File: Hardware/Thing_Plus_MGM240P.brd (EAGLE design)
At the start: 22.9 x 58.4 mm, 175 parts, among them J1 THING_PLUS_LOGICAL, J2 USB Female Type C Connector, J3 QWIIC_RIGHT_ANGLE, J5 MICRO-SDFRICTION, Q1 20V/4.2A/52mΩ/1.4W, U1 MGM240P, U2 XC6222B331MR-G, U3 EFM32GG12B410F1024GL120, U4 MCP73831, U5 MAX17048, U6 M24C02-FMC6TG, U7 MX25R8035FZUIL0, Y1 CRYSTAL-48MHZ

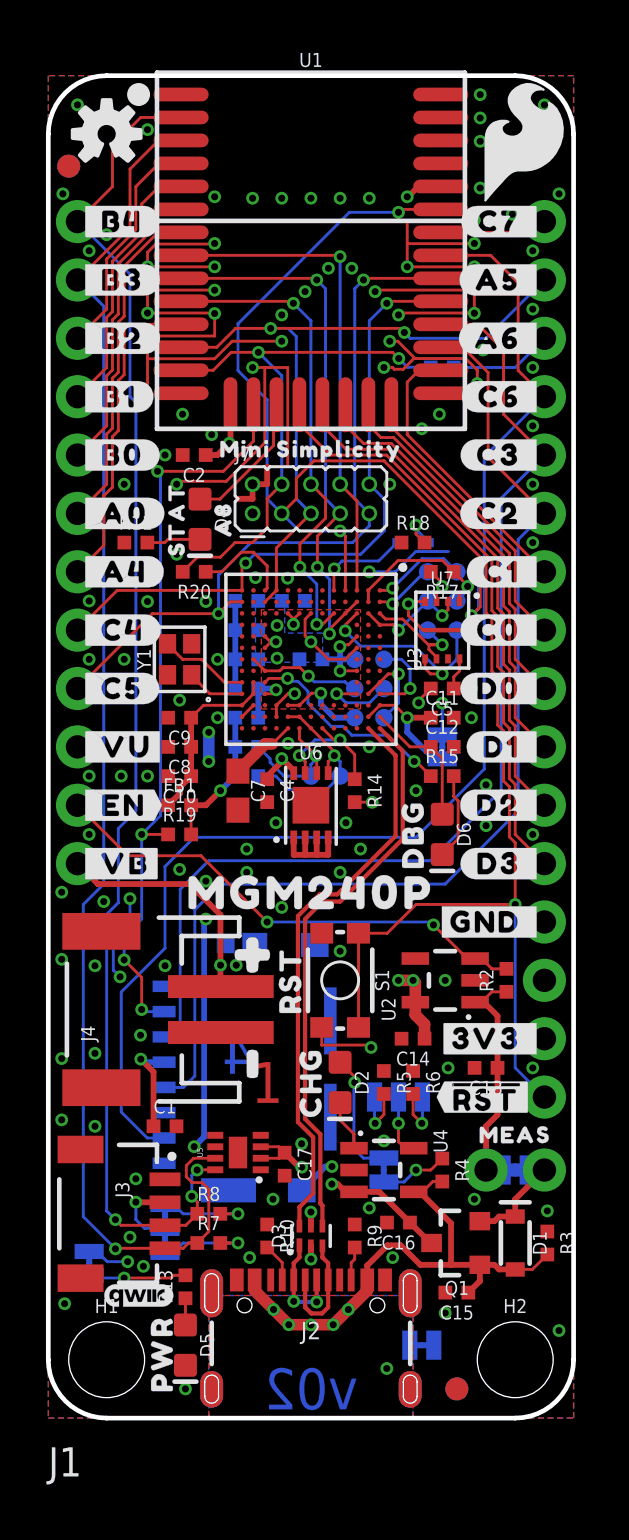
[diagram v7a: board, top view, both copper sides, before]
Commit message: Design review updates
Change voltage regulator to specify maximum input voltage only
Add Segger logo
Move traces away from jumpers to prevent accidental cutting
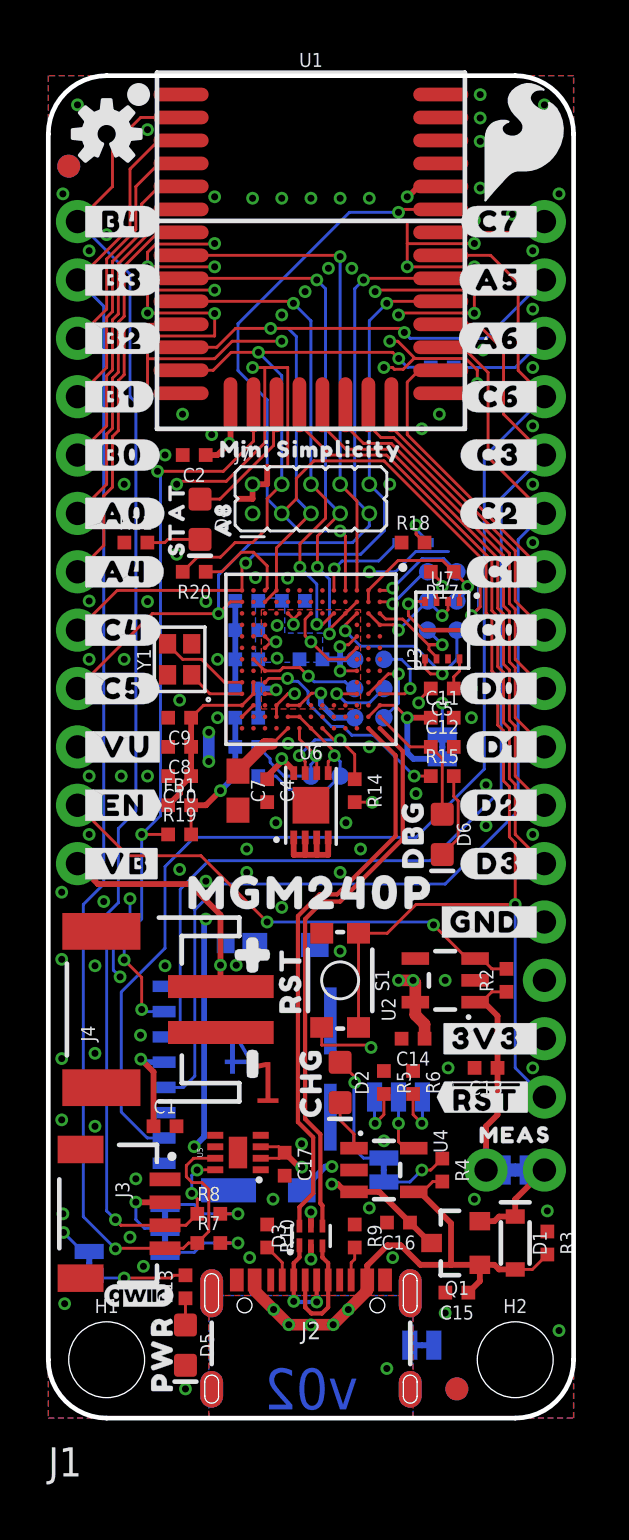
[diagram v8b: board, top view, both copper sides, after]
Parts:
- added U$65: (no value), SEGGER-LOGO:SEGGER_LOGO
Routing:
- net V_USB: track 49.6 -> 50.1 mm
- net GND: vias 136 -> 137
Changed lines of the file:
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@@
 <attribute name="VALUE" x="17.145" y="45.158" size="0.6096" layer="28" font="vector" ratio="20" rot="MR0" align="top-center"/>
 </element>
+<element name="U$65" library="SEGGER-LOGO" package="SEGGER_LOGO" value="" x="9.65" y="44.45" smashed="yes" rot="MR0"/>
 </elements>
 <signals>
@@
 <via x="13.97" y="29.21" extent="1-16" drill="0.3048"/>
 <via x="12.954" y="25.908" extent="1-16" drill="0.3048"/>
-<via x="16.002" y="27.305" extent="1-16" drill="0.3048"/>
+<via x="16.002" y="27.178" extent="1-16" drill="0.3048"/>
 <via x="10.414" y="36.5506" extent="1-16" drill="0.3048"/>
 <via x="13.97" y="36.83" extent="1-16" drill="0.3048"/>
@@
 <via x="4.318" y="35.5346" extent="1-16" drill="0.3048"/>
 <via x="21.082" y="25.4" extent="1-16" drill="0.3048"/>
+<via x="0.635" y="8.89" extent="1-16" drill="0.3048"/>
 </signal>
 <signal name="3.3V">
@@
 <wire x1="4.1569" y1="15.49" x2="4.0259" y2="15.621" width="0.254" layer="16"/>
 <via x="4.0259" y="15.621" extent="1-16" drill="0.3048"/>
-<via x="3.4544" y="6.8072" extent="1-16" drill="0.3048"/>
+<via x="0.6604" y="8.0772" extent="1-16" drill="0.3048"/>
 <contactref element="C1" pad="1"/>
 <wire x1="4.58" y1="12.7" x2="4.58" y2="15.0669" width="0.254" layer="1"/>
 <wire x1="4.58" y1="15.0669" x2="4.0259" y2="15.621" width="0.254" layer="1"/>
-<wire x1="3.4544" y1="6.8072" x2="2.5654" y2="6.8072" width="0.127" layer="16"/>
-<wire x1="2.5654" y1="6.8072" x2="2.1209" y2="7.2517" width="0.127" layer="16"/>
-<wire x1="2.1209" y1="7.2517" x2="1.778" y2="7.2517" width="0.127" layer="16"/>
+<wire x1="1.778" y1="7.2517" x2="1.4859" y2="7.2517" width="0.127" layer="16"/>
+<wire x1="1.4859" y1="7.2517" x2="0.6604" y2="8.0772" width="0.127" layer="16"/>
 <contactref element="U3" pad="L4"/>
 <contactref element="U3" pad="G3"/>
@@
 <contactref element="R19" pad="2"/>
 <wire x1="6.215" y1="25.4" x2="6.215" y2="26.67" width="0.127" layer="1"/>
+<wire x1="3.81" y1="9.398" x2="1.778" y2="7.2517" width="0" layer="19" extent="16-16"/>
 </signal>
 <signal name="V_USB">
@@
 <wire x1="15.24" y1="30.099" x2="10.414" y2="30.099" width="0.254" layer="15"/>
 <contactref element="LP" pad="2"/>
-<wire x1="17.145" y1="28.6893" x2="16.7767" y2="28.6893" width="0.254" layer="16"/>
-<wire x1="15.621" y1="29.845" x2="15.621" y2="30.48" width="0.254" layer="16"/>
-<wire x1="16.7767" y1="28.6893" x2="15.621" y2="29.845" width="0.254" layer="16"/>
+<wire x1="17.145" y1="28.6893" x2="15.8877" y2="28.6893" width="0.254" layer="16"/>
+<wire x1="15.621" y1="28.956" x2="15.621" y2="30.48" width="0.254" layer="16"/>
+<wire x1="15.8877" y1="28.6893" x2="15.621" y2="28.956" width="0.254" layer="16"/>
 </signal>
 <signal name="V_BATT">
@@
 <contactref element="R4" pad="1"/>
 <contactref element="CHG" pad="1"/>
-<wire x1="14.605" y1="10.2743" x2="15.4813" y2="10.2743" width="0.127" layer="16"/>
-<wire x1="15.4813" y1="10.2743" x2="16.002" y2="10.795" width="0.127" layer="16"/>
-<via x="16.002" y="10.795" extent="1-16" drill="0.3048"/>
-<wire x1="16.002" y1="10.795" x2="16.645" y2="10.795" width="0.127" layer="1"/>
+<wire x1="14.605" y1="10.2743" x2="15.7353" y2="10.2743" width="0.127" layer="16"/>
+<wire x1="15.7353" y1="10.2743" x2="16.256" y2="10.795" width="0.127" layer="16"/>
+<via x="16.256" y="10.795" extent="1-16" drill="0.3048"/>
+<wire x1="16.256" y1="10.795" x2="16.645" y2="10.795" width="0.127" layer="1"/>
 <wire x1="16.645" y1="10.795" x2="17.145" y2="11.295" width="0.127" layer="1"/>
 </signal>
@@
 <wire x1="7.485" y1="7.62" x2="8.255" y2="7.62" width="0.127" layer="1"/>
 <via x="8.255" y="7.62" extent="1-16" drill="0.3048"/>
-<wire x1="8.255" y1="7.62" x2="5.8674" y2="7.62" width="0.127" layer="16"/>
-<wire x1="5.8674" y1="7.62" x2="5.461" y2="7.2136" width="0.127" layer="16"/>
-<wire x1="5.461" y1="7.2136" x2="5.08" y2="7.2136" width="0.127" layer="16"/>
+<wire x1="8.255" y1="7.62" x2="6.7564" y2="7.62" width="0.127" layer="16"/>
+<wire x1="6.7564" y1="7.62" x2="6.35" y2="7.2136" width="0.127" layer="16"/>
+<wire x1="6.35" y1="7.2136" x2="5.08" y2="7.2136" width="0.127" layer="16"/>
 </signal>
 <signal name="N$13">
@@
 <wire x1="7.485" y1="8.89" x2="8.255" y2="8.89" width="0.127" layer="1"/>
 <via x="8.255" y="8.89" extent="1-16" drill="0.3048"/>
-<wire x1="8.255" y1="8.89" x2="5.8674" y2="8.89" width="0.127" layer="16"/>
-<wire x1="5.8674" y1="8.89" x2="5.461" y2="9.2964" width="0.127" layer="16"/>
-<wire x1="5.461" y1="9.2964" x2="5.08" y2="9.2964" width="0.127" layer="16"/>
+<wire x1="8.255" y1="8.89" x2="6.7564" y2="8.89" width="0.127" layer="16"/>
+<wire x1="6.7564" y1="8.89" x2="6.35" y2="9.2964" width="0.127" layer="16"/>
+<wire x1="6.35" y1="9.2964" x2="5.08" y2="9.2964" width="0.127" layer="16"/>
 </signal>
 <signal name="SCK/PC02">
@@
 <contactref element="U5" pad="8"/>
 <wire x1="3.81" y1="26.416" x2="3.81" y2="44.196" width="0.127" layer="16"/>
-<wire x1="6.485" y1="9.4106" x2="6.2436" y2="9.652" width="0.127" layer="1"/>
-<wire x1="6.485" y1="9.4106" x2="6.485" y2="8.89" width="0.127" layer="1"/>
-<via x="6.2436" y="9.652" extent="1-16" drill="0.3048"/>
-<wire x1="6.2436" y1="9.652" x2="6.2436" y2="10.5616" width="0.127" layer="16"/>
+<wire x1="6.485" y1="9.5376" x2="6.2436" y2="9.779" width="0.127" layer="1"/>
+<wire x1="6.485" y1="9.5376" x2="6.485" y2="8.89" width="0.127" layer="1"/>
+<via x="6.2436" y="9.779" extent="1-16" drill="0.3048"/>
+<wire x1="6.2436" y1="9.779" x2="6.2436" y2="10.5616" width="0.127" layer="16"/>
 <wire x1="6.2436" y1="10.5616" x2="6.477" y2="10.795" width="0.127" layer="16"/>
 <via x="6.477" y="10.795" extent="1-16" drill="0.3048"/>
@@
 <wire x1="9.598971875" y1="32.188971875" x2="10.411503125" y2="32.188971875" width="0.127" layer="1"/>
 <via x="10.411503125" y="32.188971875" extent="1-16" drill="0.3048"/>
-<wire x1="14.78153125" y1="29.718" x2="15.92453125" y2="28.575" width="0.127" layer="16"/>
-<via x="15.92453125" y="28.575" extent="1-16" drill="0.3048"/>
+<wire x1="14.14653125" y1="29.718" x2="15.92453125" y2="27.94" width="0.127" layer="16"/>
+<via x="15.92453125" y="27.94" extent="1-16" drill="0.3048"/>
 <wire x1="13.208" y1="29.718" x2="12.827" y2="30.099" width="0.127" layer="16"/>
 <wire x1="11.303" y1="31.623" x2="10.864028125" y2="32.061971875" width="0.127" layer="16"/>
 <wire x1="10.864028125" y1="32.061971875" x2="10.538503125" y2="32.061971875" width="0.127" layer="16"/>
 <wire x1="10.411503125" y1="32.188971875" x2="10.538503125" y2="32.061971875" width="0.127" layer="16"/>
-<wire x1="14.78153125" y1="29.718" x2="13.208" y2="29.718" width="0.127" layer="16"/>
+<wire x1="14.14653125" y1="29.718" x2="13.208" y2="29.718" width="0.127" layer="16"/>
 <wire x1="12.827" y1="30.099" x2="12.319" y2="30.099" width="0.127" layer="16"/>
 <wire x1="11.303" y1="31.115" x2="11.303" y2="31.623" width="0.127" layer="16"/>
 <wire x1="12.319" y1="30.099" x2="11.303" y2="31.115" width="0.127" layer="16"/>
-<wire x1="15.92453125" y1="28.575" x2="16.01" y2="28.575" width="0.127" layer="1"/>
-<wire x1="16.01" y1="28.575" x2="16.645" y2="27.94" width="0.127" layer="1"/>
+<wire x1="15.92453125" y1="27.94" x2="16.645" y2="27.94" width="0.127" layer="1"/>
 </signal>
 <signal name="N$21">
